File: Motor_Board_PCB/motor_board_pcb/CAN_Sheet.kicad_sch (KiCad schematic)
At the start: 14 parts, among them J6 CAN_OUT, U1 MCP2515-xST, U2 TJA1050, Y1 20M

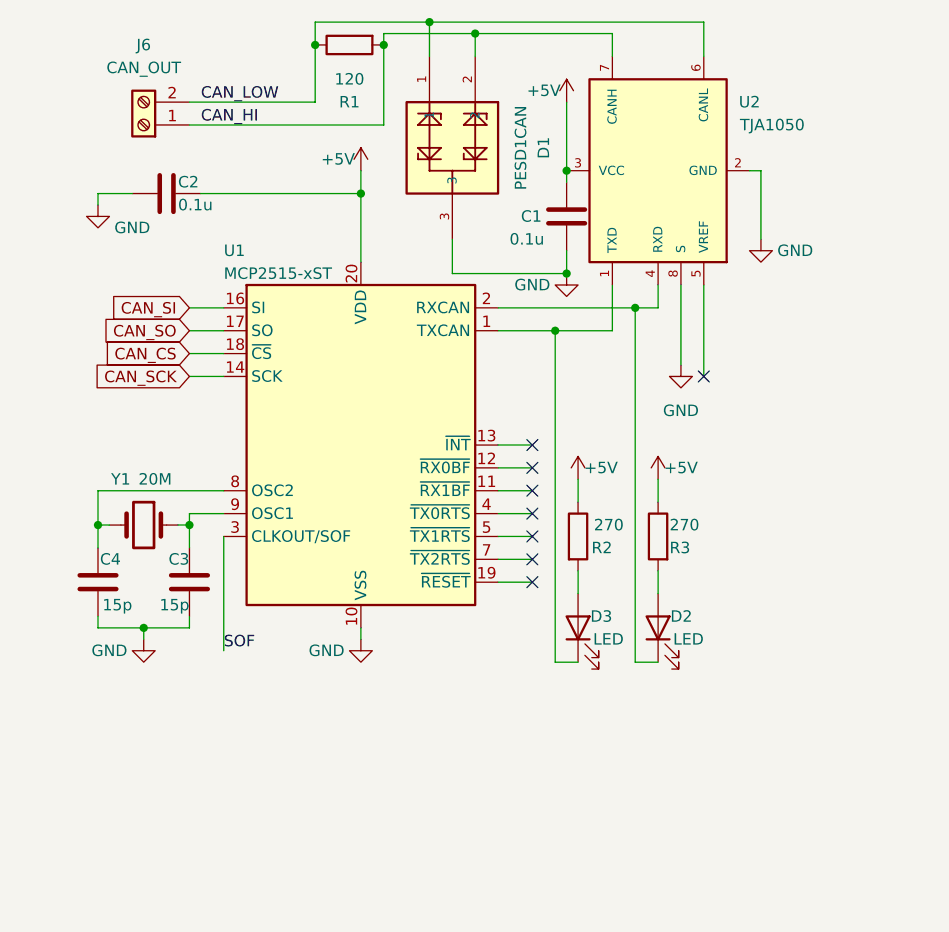
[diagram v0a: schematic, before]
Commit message: Added footprints for almost all components
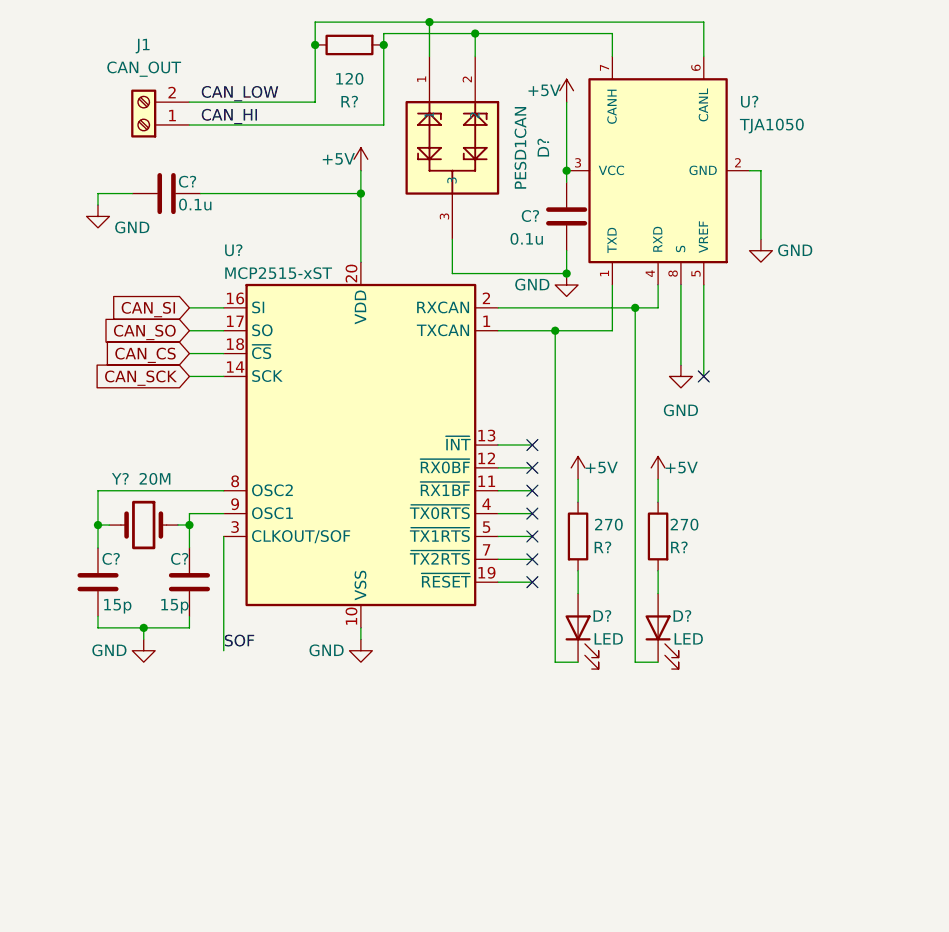
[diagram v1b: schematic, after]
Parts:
- J1: renamed from J6; footprint (none) -> Connector_PinHeader_2.54mm:PinHeader_1x02_P2.54mm_Vertical
- renumbered C2 to C?, C1 to C?, C3 to C?, C4 to C?, D3 to D?, D2 to D?, D1 to D?, R2 to R?, R3 to R?, R1 to R?, U2 to U?, U1 to U?, Y1 to Y?

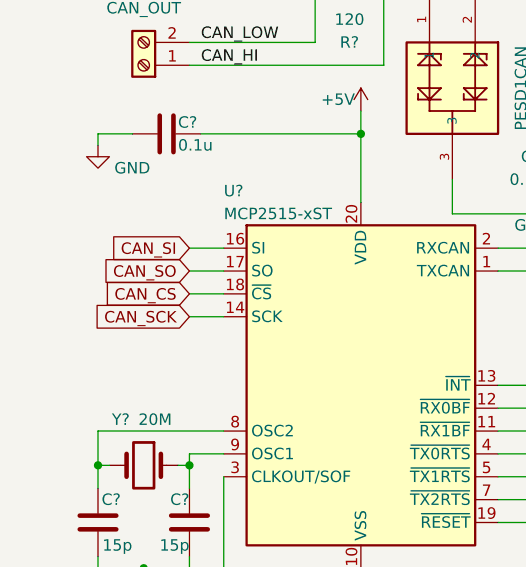
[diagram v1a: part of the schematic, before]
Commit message: Started Layout (hub board)
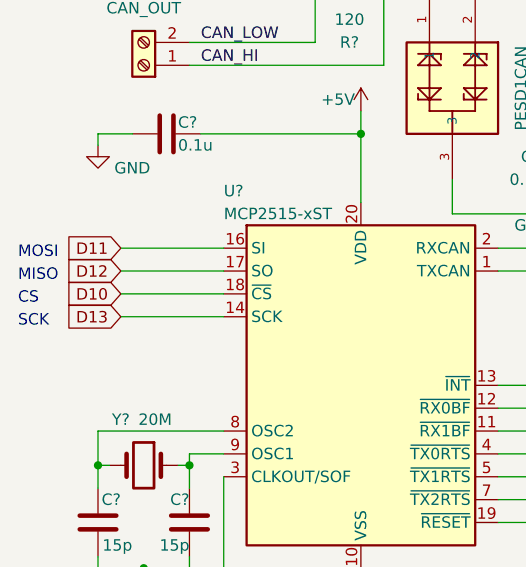
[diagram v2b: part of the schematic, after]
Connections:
- net CAN_CS renamed D10
- net CAN_SCK renamed D13
- net CAN_SI renamed D11
- net CAN_SO renamed D12
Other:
- note added: "CS"
- note added: "MISO"
- note added: "MOSI"
- note added: "SCK"
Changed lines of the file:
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@@
     (stroke (width 0) (type default))
   )
-  (wire (pts (xy 33.02 52.07) (xy 36.83 52.07))
+  (wire (pts (xy 25.4 52.07) (xy 36.83 52.07))
     (stroke (width 0) (type default))
   )
@@
     (stroke (width 0) (type default))
   )
-  (wire (pts (xy 33.02 54.61) (xy 36.83 54.61))
+  (wire (pts (xy 25.4 54.61) (xy 36.83 54.61))
     (stroke (width 0) (type default))
   )
@@
     (stroke (width 0) (type default))
   )
-  (wire (pts (xy 33.02 57.15) (xy 36.83 57.15))
+  (wire (pts (xy 25.4 57.15) (xy 36.83 57.15))
     (stroke (width 0) (type default))
   )
@@
     (stroke (width 0) (type default))
   )
-  (wire (pts (xy 33.02 59.69) (xy 36.83 59.69))
+  (wire (pts (xy 25.4 59.69) (xy 36.83 59.69))
     (stroke (width 0) (type default))
   )
@@
     (stroke (width 0) (type default))
   )
+  (text "SCK\n" (at 13.97 60.96 0)
+    (effects (font (size 1.27 1.27)) (justify left bottom))
+  )
+  (text "MISO\n" (at 13.97 55.88 0)
+    (effects (font (size 1.27 1.27)) (justify left bottom))
+  )
+  (text "MOSI" (at 13.97 53.34 0)
+    (effects (font (size 1.27 1.27)) (justify left bottom))
+  )
+  (text "CS" (at 13.97 58.42 0)
+    (effects (font (size 1.27 1.27)) (justify left bottom))
+  )
   (label "CAN_HI" (at 34.29 31.75 0) (fields_autoplaced)
     (effects (font (size 1.27 1.27)) (justify left bottom))
@@
     (effects (font (size 1.27 1.27)) (justify left bottom))
   )
-  (global_label "CAN_SI" (shape input) (at 33.02 52.07 180) (fields_autoplaced)
+  (global_label "D13" (shape input) (at 25.4 59.69 180) (fields_autoplaced)
     (effects (font (size 1.27 1.27)) (justify right))
-    (property "Intersheetrefs" "${INTERSHEET_REFS}" (at 23.1502 52.07 0)
+    (property "Intersheetrefs" "${INTERSHEET_REFS}" (at 18.8852 59.69 0)
       (effects (font (size 1.27 1.27)) (justify right) hide)
     )
   )
-  (global_label "CAN_SCK" (shape input) (at 33.02 59.69 180) (fields_autoplaced)
+  (global_label "D10" (shape input) (at 25.4 57.15 180) (fields_autoplaced)
     (effects (font (size 1.27 1.27)) (justify right))
-    (property "Intersheetrefs" "${INTERSHEET_REFS}" (at 20.9789 59.69 0)
+    (property "Intersheetrefs" "${INTERSHEET_REFS}" (at 18.8852 57.15 0)
       (effects (font (size 1.27 1.27)) (justify right) hide)
     )
   )
-  (global_label "CAN_CS" (shape input) (at 33.02 57.15 180) (fields_autoplaced)
+  (global_label "D12" (shape input) (at 25.4 54.61 180) (fields_autoplaced)
     (effects (font (size 1.27 1.27)) (justify right))
-    (property "Intersheetrefs" "${INTERSHEET_REFS}" (at 22.4591 57.15 0)
+    (property "Intersheetrefs" "${INTERSHEET_REFS}" (at 18.8852 54.61 0)
       (effects (font (size 1.27 1.27)) (justify right) hide)
     )
   )
-  (global_label "CAN_SO" (shape input) (at 33.02 54.61 180) (fields_autoplaced)
+  (global_label "D11" (shape input) (at 25.4 52.07 180) (fields_autoplaced)
     (effects (font (size 1.27 1.27)) (justify right))
-    (property "Intersheetrefs" "${INTERSHEET_REFS}" (at 22.3611 54.61 0)
+    (property "Intersheetrefs" "${INTERSHEET_REFS}" (at 18.8852 52.07 0)
       (effects (font (size 1.27 1.27)) (justify right) hide)
     )

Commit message: Schematic changes before sending to kim
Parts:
- added TP?: TestPoint, TestPoint:TestPoint_Pad_D1.0mm, symbol Connector:TestPoint
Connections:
- net at U?.19 (~{RESET}): now also TP?.1
- no-connect marks 8 -> 7
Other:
- moved on the sheet: C?, D?, R?, U?, Y?

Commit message: Meeting layout updates
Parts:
- added R7: 0, Resistor_SMD:R_0402_1005Metric, symbol Device:R
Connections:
- net D12: now also R7.1; no longer U?.17 (SO)
- new net: R7.2, U?.17 (SO)
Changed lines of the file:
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@@
-    (stroke (width 0) (type default))
-  )
-  (wire (pts (xy 25.4 78.74) (xy 36.83 78.74))
     (stroke (width 0) (type default))
   )
@@
   )
   (wire (pts (xy 85.09 29.21) (xy 85.09 36.83))
+    (stroke (width 0) (type default))
+  )
+  (wire (pts (xy 25.4 78.74) (xy 29.21 78.74))
     (stroke (width 0) (type default))
   )
@@
         )
       )
+    )
+  )
+  (symbol (lib_id "Device:R") (at 33.02 78.74 90) (mirror x) (unit 1)
+    (in_bom yes) (on_board yes) (dnp no)
+    (property "Reference" "R7" (at 27.94 80.01 90)
+      (effects (font (size 1.27 1.27)))
+    )
+    (property "Value" "0" (at 36.83 77.47 90)
+      (effects (font (size 1.27 1.27)))
+    )
+    (property "Footprint" "Resistor_SMD:R_0402_1005Metric" (at 33.02 76.962 90)
+      (effects (font (size 1.27 1.27)) hide)
+    )
+    (property "Datasheet" "~" (at 33.02 78.74 0)
+      (effects (font (size 1.27 1.27)) hide)
+    )
+    (pin "1")
+    (pin "2")
+    (instances
+      (project "central_hub"
+        (path "/0d9ec66e-0fbf-4d12-9b83-adf78971a00b/a9a7affa-d8a7-4dcd-8fe3-0de6a2b29bd6"
+          (reference "R7") (unit 1)
+        )
+        (path "/0d9ec66e-0fbf-4d12-9b83-adf78971a00b/4fb60496-ee10-4e45-a75e-a49c2c8afc68"
+          (reference "R35") (unit 1)
+        )
+      )
+      (project "motor_board_pcb"
+        (path "/4ad82a24-c992-45c9-b523-12e12bcd6ced"
+          (reference "R?") (unit 1)
+        )
+        (path "/4ad82a24-c992-45c9-b523-12e12bcd6ced/63c66207-e5d4-4f6f-af8f-451675dc3930"
+          (reference "R36") (unit 1)
+        )
+      )

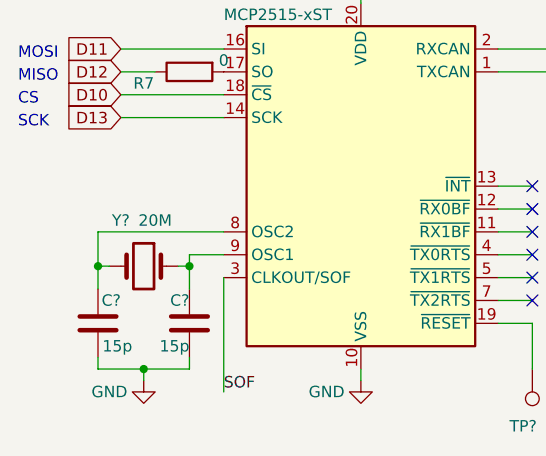
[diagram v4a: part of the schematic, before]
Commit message: Kim changes + GND pour + TearDrops + Oscillator changes
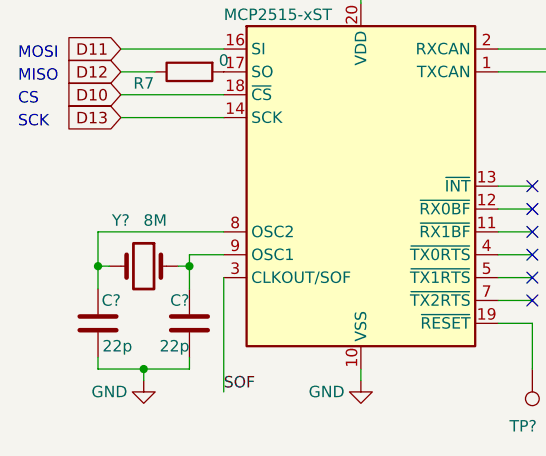
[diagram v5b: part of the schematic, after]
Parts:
- C? (x2): value 15p -> 22p
- Y?: value 20M -> 8M
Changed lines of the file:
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@@
       (effects (font (size 1.27 1.27)))
     )
-    (property "Value" "20M" (at 29.21 95.25 0)
+    (property "Value" "8M" (at 29.21 95.25 0)
       (effects (font (size 1.27 1.27)))
     )
@@
       (effects (font (size 1.27 1.27)) (justify left))
     )
-    (property "Value" "15p" (at 33.02 109.22 0)
+    (property "Value" "22p" (at 33.02 109.22 0)
       (effects (font (size 1.27 1.27)) (justify left))
     )
@@
       (effects (font (size 1.27 1.27)) (justify left))
     )
-    (property "Value" "15p" (at 26.67 109.22 0)
-      (effects (font (size 1.27 1.27)) (justify left))
-    )
+    (property "Value" "22p" (at 26.67 109.22 0)
+      (effects (font (size 1.27 1.27)) (justify left))
+    )

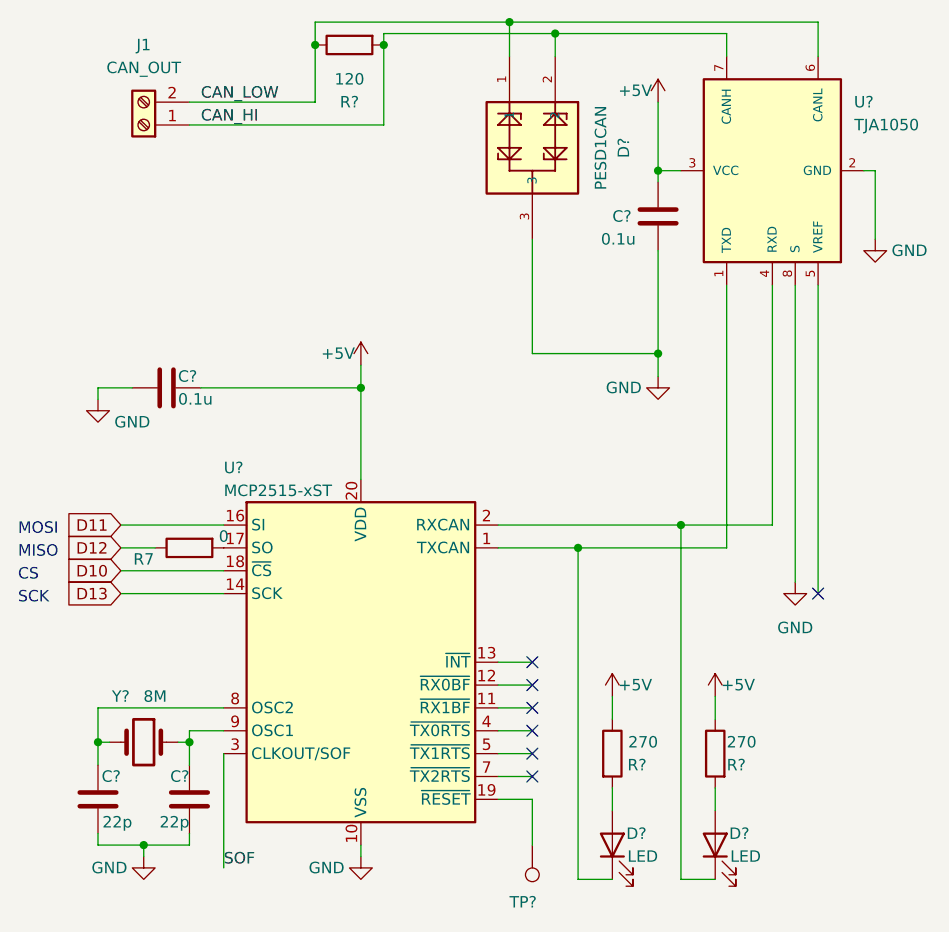
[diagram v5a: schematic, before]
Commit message: - added footprint labels to schematic symbols
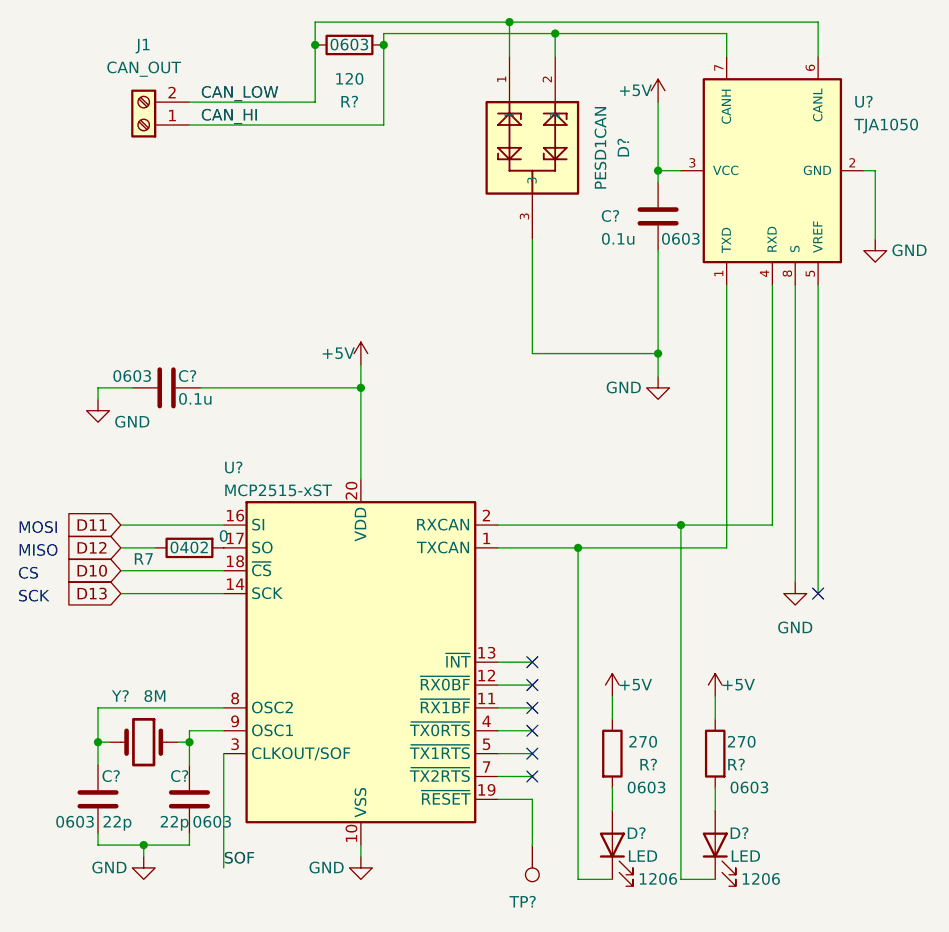
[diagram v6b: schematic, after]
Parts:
- C? (x4), R? (x3): FP (none) -> 0603
- D? (x2): FP (none) -> 1206
- R7: FP (none) -> 0402
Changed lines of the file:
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@@
       (effects (font (size 1.27 1.27)) hide)
+    )
+    (property "FP" "0603" (at 26.67 59.69 90)
+      (effects (font (size 1.27 1.27)))
     )
     (pin "1")
@@
   (symbol (lib_id "Device:C") (at 85.09 41.91 0) (unit 1)
     (in_bom yes) (on_board yes) (dnp no)
-    (property "Reference" "C?" (at 80.01 41.91 0)
+    (property "Reference" "C?" (at 78.74 41.91 0)
       (effects (font (size 1.27 1.27)) (justify left))
     )
@@
       (effects (font (size 1.27 1.27)) hide)
     )
+    (property "FP" "0603" (at 87.63 44.45 0)
+      (effects (font (size 1.27 1.27)))
+    )
     (pin "1")
     (pin "2")
@@
       (effects (font (size 1.27 1.27)) hide)
     )
+    (property "FP" "1206" (at 85.09 115.57 90)
+      (effects (font (size 1.27 1.27)))
+    )
     (pin "1")
     (pin "2")
@@
       (effects (font (size 1.27 1.27)) hide)
     )
+    (property "FP" "0603" (at 35.56 109.22 0)
+      (effects (font (size 1.27 1.27)))
+    )
     (pin "1")
     (pin "2")
@@
       (effects (font (size 1.27 1.27)) hide)
     )
+    (property "FP" "1206" (at 96.52 115.57 90)
+      (effects (font (size 1.27 1.27)))
+    )
     (pin "1")
     (pin "2")
@@
   (symbol (lib_id "Device:R") (at 80.01 101.6 0) (unit 1)
     (in_bom yes) (on_board yes) (dnp no)
-    (property "Reference" "R?" (at 83.82 102.87 0)
+    (property "Reference" "R?" (at 85.09 102.87 0)
       (effects (font (size 1.27 1.27)) (justify right))
     )
@@
     (property "Datasheet" "~" (at 80.01 101.6 0)
       (effects (font (size 1.27 1.27)) hide)
+    )
+    (property "FP" "0603" (at 83.82 105.41 0)
+      (effects (font (size 1.27 1.27)))
     )
     (pin "1")
@@
       (effects (font (size 1.27 1.27)) hide)
     )
+    (property "FP" "0402" (at 33.02 78.74 90)
+      (effects (font (size 1.27 1.27)))
+    )
     (pin "1")
     (pin "2")
@@
       (effects (font (size 1.27 1.27)) hide)
     )
+    (property "FP" "0603" (at 95.25 105.41 0)
+      (effects (font (size 1.27 1.27)))
+    )
     (pin "1")
     (pin "2")
@@
     (property "Datasheet" "~" (at 22.86 106.68 0)
       (effects (font (size 1.27 1.27)) hide)
+    )
+    (property "FP" "0603" (at 20.32 109.22 0)
+      (effects (font (size 1.27 1.27)))
     )
     (pin "1")
@@
       (effects (font (size 1.27 1.27)) hide)
     )
-    (pin "1")
+    (property "FP" "0603" (at 50.8 22.86 90)
+      (effects (font (size 1.27 1.27)))
+    )
+    (pin "1")
